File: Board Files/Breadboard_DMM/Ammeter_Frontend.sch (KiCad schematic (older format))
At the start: 6 parts

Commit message: Started adding Digikey links
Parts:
- D701, D702, D703, D704: Digi-Key Link (none) -> https://www.digikey.com/en/products/detail/smc-diode-soluti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; Digi-Key PN - -> 1655-1N4007FLCT-ND
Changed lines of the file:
@@
 $Descr A4 11693 8268
 encoding utf-8
-Sheet 7 10
-Title ""
-Date ""
-Rev ""
+Sheet 7 11
+Title "Toast-O-Meter"
+Date "2020-08-14"
+Rev "0"
 Comp ""
 Comment1 ""
@@
 F 2 "Diode_SMD:D_SOD-123" H 5850 3450 50  0001 C CNN
 F 3 "http://www.smc-diodes.com/propdf/1N4001FL-1N4007FL%20N1646%20REV.A.pdf" H 5850 3450 50  0001 C CNN
-F 4 "" H 5850 3450 50  0001 C CNN "Digi-Key Link"
-F 5 "-" H 5850 3450 50  0001 C CNN "Digi-Key PN"
+F 4 "https://www.digikey.com/en/products/detail/smc-diode-solutions/1N4007FLTR/11657817" H 5850 3450 50  0001 C CNN "Digi-Key Link"
+F 5 "1655-1N4007FLCT-ND" H 5850 3450 50  0001 C CNN "Digi-Key PN"
 	1    5850 3450
 	-1   0    0    -1
@@
 F 2 "Diode_SMD:D_SOD-123" H 6450 3450 50  0001 C CNN
 F 3 "http://www.smc-diodes.com/propdf/1N4001FL-1N4007FL%20N1646%20REV.A.pdf" H 6450 3450 50  0001 C CNN
-F 4 "" H 6450 3450 50  0001 C CNN "Digi-Key Link"
-F 5 "-" H 6450 3450 50  0001 C CNN "Digi-Key PN"
+F 4 "https://www.digikey.com/en/products/detail/smc-diode-solutions/1N4007FLTR/11657817" H 6450 3450 50  0001 C CNN "Digi-Key Link"
+F 5 "1655-1N4007FLCT-ND" H 6450 3450 50  0001 C CNN "Digi-Key PN"
 	1    6450 3450
 	-1   0    0    -1
@@
 F 2 "Diode_SMD:D_SOD-123" H 6450 4100 50  0001 C CNN
 F 3 "http://www.smc-diodes.com/propdf/1N4001FL-1N4007FL%20N1646%20REV.A.pdf" H 6450 4100 50  0001 C CNN
-F 4 "" H 6450 4100 50  0001 C CNN "Digi-Key Link"
-F 5 "-" H 6450 4100 50  0001 C CNN "Digi-Key PN"
+F 4 "https://www.digikey.com/en/products/detail/smc-diode-solutions/1N4007FLTR/11657817" H 6450 4100 50  0001 C CNN "Digi-Key Link"
+F 5 "1655-1N4007FLCT-ND" H 6450 4100 50  0001 C CNN "Digi-Key PN"
 	1    6450 4100
 	-1   0    0    -1
@@
 F 2 "Diode_SMD:D_SOD-123" H 5850 4100 50  0001 C CNN
 F 3 "http://www.smc-diodes.com/propdf/1N4001FL-1N4007FL%20N1646%20REV.A.pdf" H 5850 4100 50  0001 C CNN
-F 4 "" H 5850 4100 50  0001 C CNN "Digi-Key Link"
-F 5 "-" H 5850 4100 50  0001 C CNN "Digi-Key PN"
+F 4 "https://www.digikey.com/en/products/detail/smc-diode-solutions/1N4007FLTR/11657817" H 5850 4100 50  0001 C CNN "Digi-Key Link"
+F 5 "1655-1N4007FLCT-ND" H 5850 4100 50  0001 C CNN "Digi-Key PN"
 	1    5850 4100
 	-1   0    0    -1

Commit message: Finished adding parts, cleaned up, ran ERC
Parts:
- F701: Digi-Key Link (none) -> https://www.digikey.com/en/products/detail/littelfuse-inc/0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; Digi-Key PN - -> F6094-ND; F11153-ND
- R701: footprint (none) -> Resistor_SMD:R_Shunt_Ohmite_LVK24; Digi-Key Link (none) -> https://www.digikey.com/en/products/detail/ohmite/LVK24R100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; Digi-Key PN - -> 273-LVK24R100CERDKR-ND; Tolerance 0.1% -> 0.25%
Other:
- moved on the sheet: D701, D702, D703, D704, F701, R701

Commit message: Cleaned up files
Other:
- note added: "Ammeter Frontend"
- note removed: "Ammeter Input"
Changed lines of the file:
@@
 	0    1    1    0
 $EndComp
-Wire Wire Line
-	5850 4550 6250 4550
 Text Notes 12450 9750 0    200  ~ 40
-Ammeter Input
+Ammeter Frontend
 Text HLabel 10050 5700 2    50   Output ~ 0
 I_SENSE-
@@
 Wire Wire Line
 	8500 5700 10050 5700
-Text HLabel 5850 4550 0    50   Input ~ 0
-INPUT_I+
 Text HLabel 5850 5700 0    50   Input ~ 0
 INPUT_I-
@@
 	7150 5700 5850 5700
 Connection ~ 7150 5700
+Text HLabel 5850 4550 0    50   Input ~ 0
+INPUT_I+
+Wire Wire Line
+	5850 4550 6250 4550
 $EndSCHEMATC

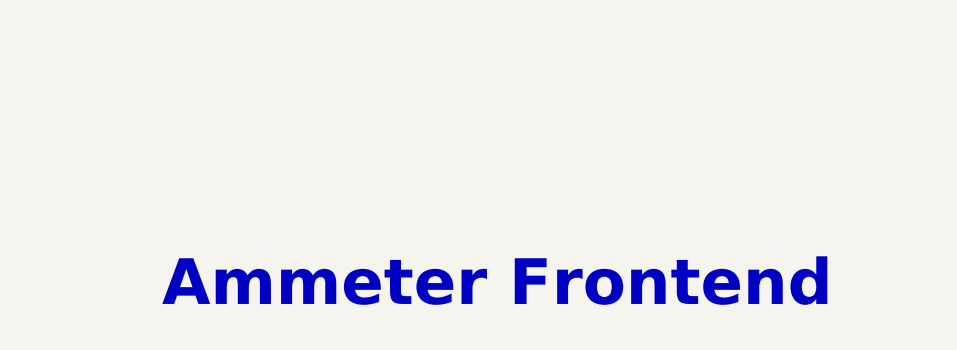
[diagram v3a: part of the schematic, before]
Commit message: Updated probe connector arrangement
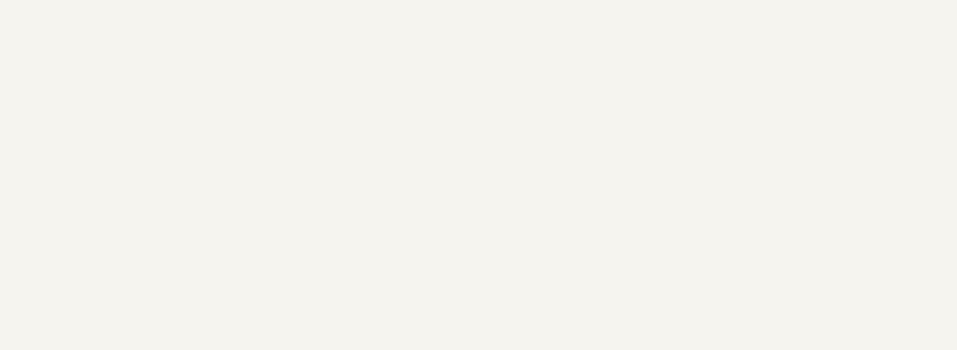
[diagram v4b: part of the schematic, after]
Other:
- note removed: "Ammeter Frontend"
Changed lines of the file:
@@
 Sheet 6 8
 Title "Toast-O-Meter"
-Date "2020-08-14"
+Date "2020-10-06"
 Rev "0"
 Comp ""
-Comment1 ""
+Comment1 "Isaac Rex"
 Comment2 ""
 Comment3 ""
@@
 	0    1    1    0
 $EndComp
-Text Notes 12450 9750 0    200  ~ 40
-Ammeter Frontend
 Text HLabel 10050 5700 2    50   Output ~ 0
 I_SENSE-

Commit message: Semi-finished component placement
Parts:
- D601: renamed from D701; symbol Device:D_ALT -> Device:D_Filled
- D602: renamed from D702; symbol Device:D_ALT -> Device:D_Filled
- D603: renamed from D703; symbol Device:D_ALT -> Device:D_Filled
- D604: renamed from D704; symbol Device:D_ALT -> Device:D_Filled
- F601: renamed from F701; value 3.15A -> 2.0A; footprint irex_Fuse:Fuseholder_Cylinder-5x20mm_Littlefuse_0PTF0078P_Horizontal_Open -> Fuse:Fuseholder_Littelfuse_Nano2_154x; Digi-Key Link https://www.digikey.com/en/products/detail/littelfuse-inc/0PTF0078P/3427168 ; https://www.digikey.com/en/products/detail/littelfuse-inc/06173.15MXP/5233771 -> https://www.digikey.com/en/products/detail/littelfuse-inc/0154002-DR/183354; Digi-Key PN F6094-ND; F11153-ND -> F1224TR-ND
- renumbered R701 to R601
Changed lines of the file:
@@
 P 6400 4550
 AR Path="/5F511849/5FE50BA2" Ref="F?"  Part="1"
-AR Path="/5F511849/5FE469BC/5FE50BA2" Ref="F701"  Part="1"
-F 0 "F701" V 6203 4550 50  0000 C CNN
-F 1 "3.15A" V 6294 4550 50  0000 C CNN
-F 2 "irex_Fuse:Fuseholder_Cylinder-5x20mm_Littlefuse_0PTF0078P_Horizontal_Open" V 6330 4550 50  0001 C CNN
-F 3 "https://media.digikey.com/pdf/Data%20Sheets/Littelfuse%20PDFs/617Series_Fuse_DS_v1%200.pdf~" H 6400 4550 50  0001 C CNN
-F 4 "https://www.digikey.com/en/products/detail/littelfuse-inc/0PTF0078P/3427168 ; https://www.digikey.com/en/products/detail/littelfuse-inc/06173.15MXP/5233771" H 6400 4550 50  0001 C CNN "Digi-Key Link"
-F 5 "F6094-ND; F11153-ND" H 6400 4550 50  0001 C CNN "Digi-Key PN"
+AR Path="/5F511849/5FE469BC/5FE50BA2" Ref="F601"  Part="1"
+F 0 "F601" V 6203 4550 50  0000 C CNN
+F 1 "2.0A" V 6294 4550 50  0000 C CNN
+F 2 "Fuse:Fuseholder_Littelfuse_Nano2_154x" V 6330 4550 50  0001 C CNN
+F 3 "https://www.littelfuse.com/~/media/electronics/datasheets/fuses/littelfuse_fuse_154_154t_154l_154tl_datasheet.pdf.pdf" H 6400 4550 50  0001 C CNN
+F 4 "https://www.digikey.com/en/products/detail/littelfuse-inc/0154002-DR/183354" H 6400 4550 50  0001 C CNN "Digi-Key Link"
+F 5 "F1224TR-ND" H 6400 4550 50  0001 C CNN "Digi-Key PN"
 	1    6400 4550
 	0    1    1    0
@@
 I_SENSE+
 $Comp
-L Device:D_ALT D?
+L Device:D_Filled D?
 U 1 1 5FE50BB4
 P 8200 4850
 AR Path="/5F511849/5FE50BB4" Ref="D?"  Part="1"
-AR Path="/5F511849/5FE469BC/5FE50BB4" Ref="D701"  Part="1"
-F 0 "D701" H 8150 5050 50  0000 L CNN
+AR Path="/5F511849/5FE469BC/5FE50BB4" Ref="D601"  Part="1"
+AR Path="/5FE50BB4" Ref="D?"  Part="1"
+F 0 "D601" H 8150 5050 50  0000 L CNN
 F 1 "1N4007" H 8050 4950 50  0000 L CNN
 F 2 "Diode_SMD:D_SOD-123" H 8200 4850 50  0001 C CNN
@@
 $EndComp
 $Comp
-L Device:D_ALT D?
+L Device:D_Filled D?
 U 1 1 5FE50BBA
 P 8800 4850
 AR Path="/5F511849/5FE50BBA" Ref="D?"  Part="1"
-AR Path="/5F511849/5FE469BC/5FE50BBA" Ref="D702"  Part="1"
-F 0 "D702" H 8750 5050 50  0000 L CNN
+AR Path="/5F511849/5FE469BC/5FE50BBA" Ref="D602"  Part="1"
+AR Path="/5FE50BBA" Ref="D?"  Part="1"
+F 0 "D602" H 8750 5050 50  0000 L CNN
 F 1 "1N4007" H 8650 4950 50  0000 L CNN
 F 2 "Diode_SMD:D_SOD-123" H 8800 4850 50  0001 C CNN
@@
 $EndComp
 $Comp
-L Device:D_ALT D?
+L Device:D_Filled D?
 U 1 1 5FE50BC0
 P 8800 5500
 AR Path="/5F511849/5FE50BC0" Ref="D?"  Part="1"
-AR Path="/5F511849/5FE469BC/5FE50BC0" Ref="D704"  Part="1"
-F 0 "D704" H 8750 5700 50  0000 L CNN
+AR Path="/5F511849/5FE469BC/5FE50BC0" Ref="D604"  Part="1"
+AR Path="/5FE50BC0" Ref="D?"  Part="1"
+F 0 "D604" H 8750 5700 50  0000 L CNN
 F 1 "1N4007" H 8650 5600 50  0000 L CNN
 F 2 "Diode_SMD:D_SOD-123" H 8800 5500 50  0001 C CNN
@@
 $EndComp
 $Comp
-L Device:D_ALT D?
+L Device:D_Filled D?
 U 1 1 5FE50BC6
 P 8200 5500
 AR Path="/5F511849/5FE50BC6" Ref="D?"  Part="1"
-AR Path="/5F511849/5FE469BC/5FE50BC6" Ref="D703"  Part="1"
-F 0 "D703" H 8150 5700 50  0000 L CNN
+AR Path="/5F511849/5FE469BC/5FE50BC6" Ref="D603"  Part="1"
+AR Path="/5FE50BC6" Ref="D?"  Part="1"
+F 0 "D603" H 8150 5700 50  0000 L CNN
 F 1 "1N4007" H 8050 5600 50  0000 L CNN
 F 2 "Diode_SMD:D_SOD-123" H 8200 5500 50  0001 C CNN
@@
 AR Path="/5FE50B9C" Ref="R?"  Part="1"
 AR Path="/5F511849/5FE50B9C" Ref="R?"  Part="1"
-AR Path="/5F511849/5FE469BC/5FE50B9C" Ref="R701"  Part="1"
-F 0 "R701" H 7200 5200 50  0000 L CNN
+AR Path="/5F511849/5FE469BC/5FE50B9C" Ref="R601"  Part="1"
+F 0 "R601" H 7200 5200 50  0000 L CNN
 F 1 "0.1" H 7200 5100 50  0000 L CNN
 F 2 "Resistor_SMD:R_Shunt_Ohmite_LVK24" V 7190 5090 50  0001 C CNN
